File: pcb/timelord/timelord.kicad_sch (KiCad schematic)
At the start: 33 parts, among them J1 GPIO, J2 BCKP_PWR, J3 OLED, J4 EXTERNAL, J5 SMA, Q1 BC846, Q2 BC846, U2 NEO-F10T, U3 DS3231MZ

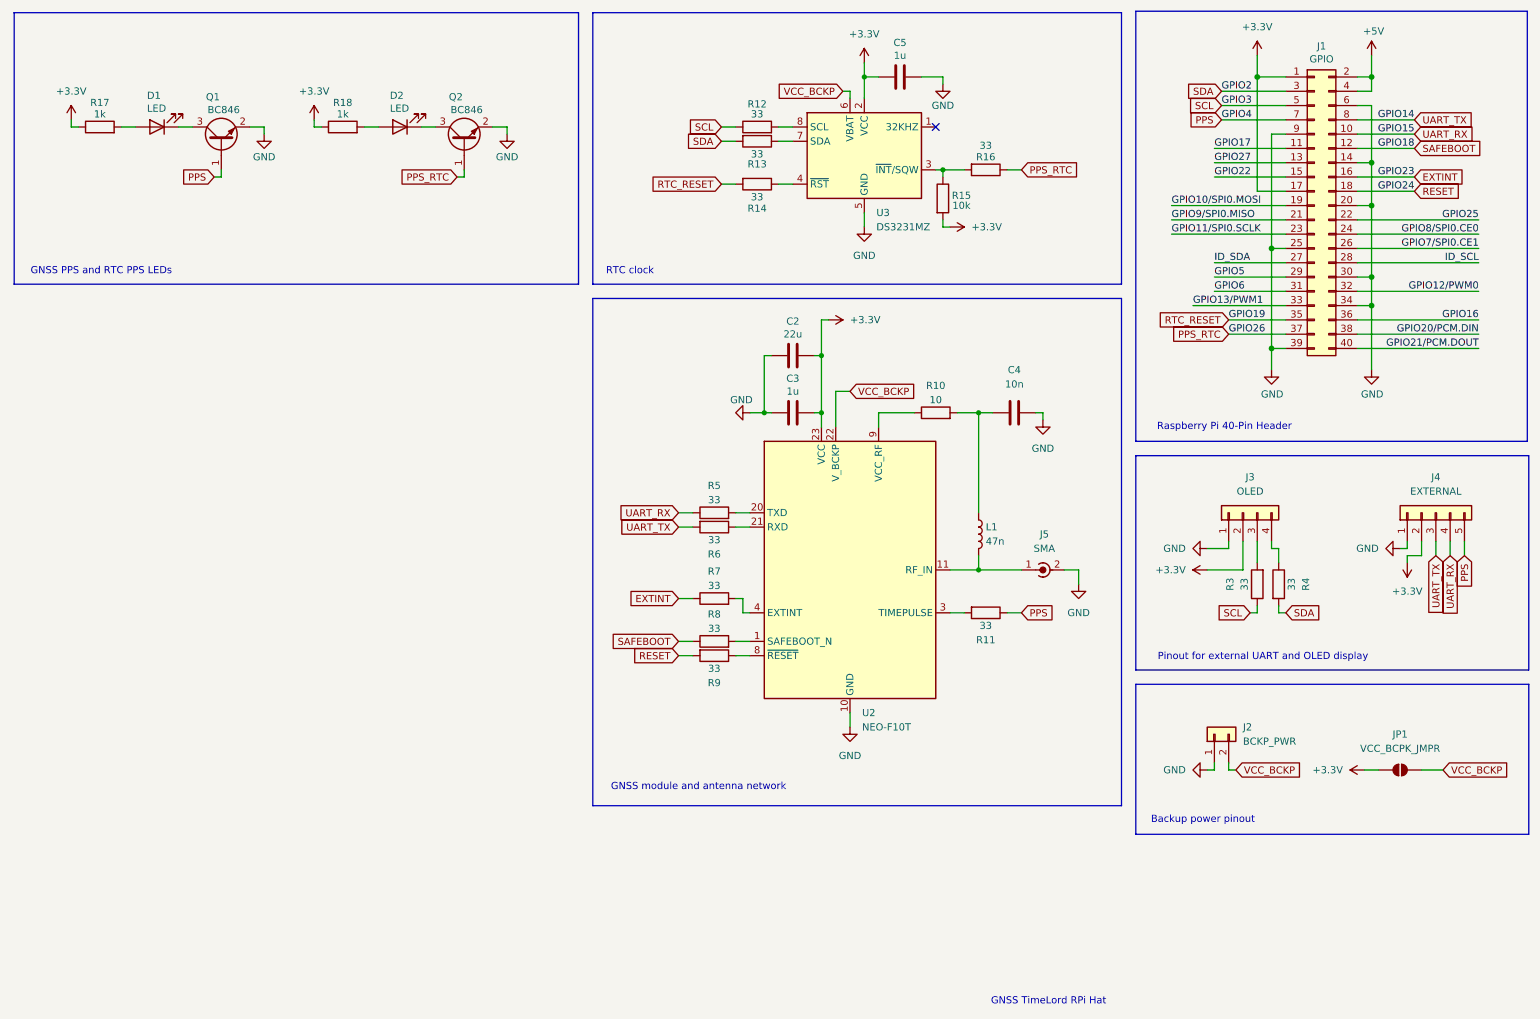
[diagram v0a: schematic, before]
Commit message: Fix MFRs and component sizing
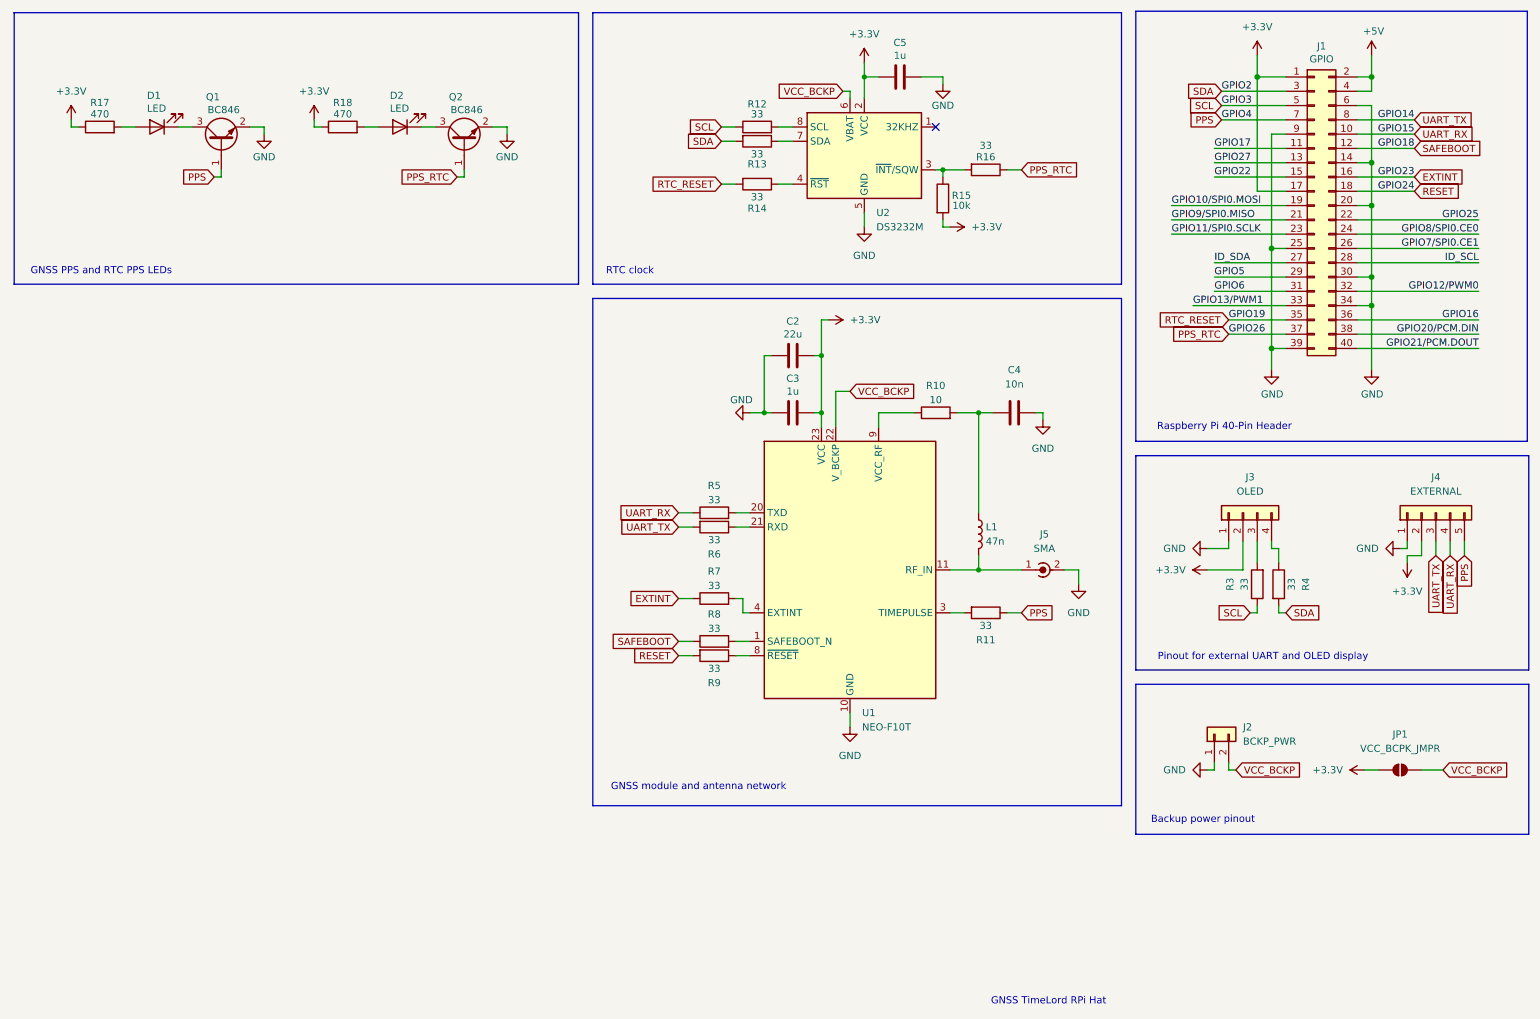
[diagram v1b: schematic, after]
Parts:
- removed U3: DS3231MZ, Package_SO:SOIC-8_3.9x4.9mm_P1.27mm, symbol Timer_RTC:DS3231MZ
- added U2: DS3232M, Package_SO:SOIC-8_3.9x4.9mm_P1.27mm, symbol Timer_RTC:DS3232M
- D1: MFR 720-KRDELPS122A5163 -> 720-KBDELPS212A6350
- J1: MFR (none) -> 485-2222
- Q1, Q2: MFR 621-1N5711W-F -> 863-BC846BLT1G
- R17, R18: value 1k -> 470; footprint Resistor_SMD:R_0805_2012Metric -> Resistor_SMD:R_0603_1608Metric; MFR 603-RT0805DRD071KL -> 603-RT0603DRD07470RL
- renumbered U2 to U1
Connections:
- net +3.3V: now also U2.2 (VCC)
- net GND: now also U2.5 (GND)
- net VCC_BCKP: now also U2.6 (VBAT)
- net at R15.1, R16.2: now also U2.3 (~{INT}/SQW)
- net at R14.1: now also U2.4 (~{RST})
- net at R13.1: now also U2.7 (SDA)
- net at R12.2: now also U2.8 (SCL)
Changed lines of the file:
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@@
 			)
 		)
+		(property "MFR" "485-2222"
+			(at 245.11 48.26 0)
+			(effects
+				(font
+					(size 1.27 1.27)
+				)
+				(hide yes)
+			)
+		)
 		(pin "1"
 		)
@@
 		(dnp no)
 		(fields_autoplaced yes)
-		(property "Reference" "U2"
+		(property "Reference" "U1"
 			(at 164.7033 138.43 0)
 			(effects
@@
 			(project ""
 				(path "/e63e39d7-6ac0-4ffd-8aa3-1841a4541b55"
-					(reference "U2")
+					(reference "U1")
 					(unit 1)
 				)
@@
 	(symbol
 		(lib_id "Device:R")
-		(at 186.69 41.91 270)
+		(at 29.21 34.29 90)
 		(unit 1)
 		(exclude_from_sim no)
@@
 		(on_board yes)
 		(dnp no)
-		(property "Reference" "R16"
-			(at 186.69 39.624 90)
+		(property "Reference" "R17"
+			(at 29.21 29.972 90)
 			(effects
 				(font
@@
 			)
 		)
-		(property "Value" "33"
-			(at 186.69 37.592 90)
+		(property "Value" "470"
+			(at 29.21 32.004 90)
 			(effects
 				(font
@@
 		)
 		(property "Footprint" "Resistor_SMD:R_0603_1608Metric"
-			(at 186.69 40.132 90)
+			(at 29.21 36.068 90)
 			(effects
 				(font
@@
 		)
 		(property "Datasheet" "~"
-			(at 186.69 41.91 0)
+			(at 29.21 34.29 0)
 			(effects
 				(font
@@
 		)
 		(property "Description" "Resistor"
-			(at 186.69 41.91 0)
+			(at 29.21 34.29 0)
 			(effects
 				(font
@@
 			)
 		)
-		(property "MFR" "603-RT0603FRE0733RL"
-			(at 186.69 41.91 90)
+		(property "MFR" "603-RT0603DRD07470RL"
+			(at 29.21 34.29 90)
 			(effects
 				(font
@@
 		)
 		(instances
-			(project ""
+			(project "timelord"
 				(path "/e63e39d7-6ac0-4ffd-8aa3-1841a4541b55"
-					(reference "R16")
+					(reference "R17")
 					(unit 1)
 				)
@@
 	)
 	(symbol
-		(lib_id "power:+3.3V")
-		(at 226.06 113.03 90)
+		(lib_id "Device:R")
+		(at 186.69 41.91 270)
 		(unit 1)
 		(exclude_from_sim no)
@@
 		(on_board yes)
 		(dnp no)
-		(fields_autoplaced yes)
-		(property "Reference" "#PWR0119"
-			(at 229.87 113.03 0)
+		(property "Reference" "R16"
+			(at 186.69 39.624 90)
 			(effects
 				(font
 					(size 1.27 1.27)
 				)
-				(hide yes)
 			)
 		)
-		(property "Value" "+3.3V"
-			(at 222.25 113.0299 90)
+		(property "Value" "33"
+			(at 186.69 37.592 90)
 			(effects
 				(font
 					(size 1.27 1.27)
 				)
-				(justify left)
 			)
 		)
-		(property "Footprint" ""
-			(at 226.06 113.03 0)
+		(property "Footprint" "Resistor_SMD:R_0603_1608Metric"
+			(at 186.69 40.132 90)
 			(effects
 				(font
@@
 			)
 		)
-		(property "Datasheet" ""
-			(at 226.06 113.03 0)
+		(property "Datasheet" "~"
+			(at 186.69 41.91 0)
 			(effects
 				(font
@@
 			)
 		)
-		(property "Description" "Power symbol creates a global label with name \"+3.3V\""
-			(at 226.06 113.03 0)
+		(property "Description" "Resistor"
+			(at 186.69 41.91 0)
+			(effects
+				(font
+					(size 1.27 1.27)
+				)
+				(hide yes)
+			)
+		)
+		(property "MFR" "603-RT0603FRE0733RL"
+			(at 186.69 41.91 90)
 			(effects
 				(font
@@
 		(pin "1"
 		)
+		(pin "2"
+		)
 		(instances
-			(project "timelord2"
+			(project ""
 				(path "/e63e39d7-6ac0-4ffd-8aa3-1841a4541b55"
-					(reference "#PWR0119")
+					(reference "R16")
 					(unit 1)
 				)
@@
 	)
 	(symbol
-		(lib_id "Device:R")
-		(at 29.21 34.29 90)
+		(lib_id "power:+3.3V")
+		(at 226.06 113.03 90)
 		(unit 1)
 		(exclude_from_sim no)
@@
 		(on_board yes)
 		(dnp no)
-		(property "Reference" "R17"
-			(at 29.21 29.972 90)
-			(effects
-				(font
-					(size 1.27 1.27)
-				)
-			)
-		)
-		(property "Value" "1k"
-			(at 29.21 32.004 90)
+		(fields_autoplaced yes)
+		(property "Reference" "#PWR0119"
+			(at 229.87 113.03 0)
 			(effects
 				(font
 					(size 1.27 1.27)
 				)
+				(hide yes)
 			)
 		)
-		(property "Footprint" "Resistor_SMD:R_0805_2012Metric"
-			(at 29.21 36.068 90)
+		(property "Value" "+3.3V"
+			(at 222.25 113.0299 90)
 			(effects
 				(font
 					(size 1.27 1.27)
 				)
-				(hide yes)
+				(justify left)
 			)
 		)
-		(property "Datasheet" "~"
-			(at 29.21 34.29 0)
+		(property "Footprint" ""
+			(at 226.06 113.03 0)
 			(effects
 				(font
@@
 			)
 		)
-		(property "Description" "Resistor"
-			(at 29.21 34.29 0)
+		(property "Datasheet" ""
+			(at 226.06 113.03 0)
 			(effects
 				(font
@@
 			)
 		)
-		(property "MFR" "603-RT0805DRD071KL"
-			(at 29.21 34.29 90)
+		(property "Description" "Power symbol creates a global label with name \"+3.3V\""
+			(at 226.06 113.03 0)
 			(effects
 				(font
@@
 		(pin "1"
 		)
-		(pin "2"
-		)
 		(instances
 			(project "timelord2"
 				(path "/e63e39d7-6ac0-4ffd-8aa3-1841a4541b55"
-					(reference "R17")
+					(reference "#PWR0119")
 					(unit 1)
 				)
@@
 			)
 		)
-		(property "MFR" "720-KRDELPS122A5163"
+		(property "MFR" "720-KBDELPS212A6350"
 			(at 39.37 34.29 0)
 			(effects
@@
 			)
 		)
-		(property "Value" "1k"
+		(property "Value" "470"
 			(at 72.39 32.004 90)
 			(effects
@@
 			)
 		)
-		(property "Footprint" "Resistor_SMD:R_0805_2012Metric"
+		(property "Footprint" "Resistor_SMD:R_0603_1608Metric"
 			(at 72.39 36.068 90)
 			(effects
@@
 			)
 		)
-		(property "MFR" "603-RT0805DRD071KL"
+		(property "MFR" "603-RT0603DRD07470RL"
 			(at 72.39 34.29 90)
 			(effects
@@
 	)
 	(symbol
-		(lib_id "Timer_RTC:DS3231MZ")
-		(at 165.1 39.37 0)
-		(unit 1)
-		(exclude_from_sim no)
-		(in_bom yes)
-		(on_board yes)
-		(dnp no)
-		(fields_autoplaced yes)
-		(property "Reference" "U3"
-			(at 167.2433 49.53 0)
-			(effects
-				(font
-					(size 1.27 1.27)
-				)
-				(justify left)
-			)
-		)
-		(property "Value" "DS3231MZ"
-			(at 167.2433 52.07 0)
-			(effects
-				(font
-					(size 1.27 1.27)
-				)
-				(justify left)
-			)
-		)
-		(property "Footprint" "Package_SO:SOIC-8_3.9x4.9mm_P1.27mm"
-			(at 165.1 52.07 0)
-			(effects
-				(font
-					(size 1.27 1.27)
-				)
-				(hide yes)
-			)
-		)
-		(property "Datasheet" "http://datasheets.maximintegrated.com/en/ds/DS3231M.pdf"
-			(at 165.1 54.61 0)
-			(effects
-				(font
-					(size 1.27 1.27)
-				)
-				(hide yes)
-			)
-		)
-		(property "Description" "±5ppm, I2C Real-Time Clock SOIC-8"
-			(at 165.1 39.37 0)
-			(effects
-				(font
-					(size 1.27 1.27)
-				)
-				(hide yes)
-			)
-		)
-		(pin "6"
-		)
-		(pin "8"
-		)
-		(pin "2"
-		)
-		(pin "5"
-		)
-		(pin "4"
-		)
-		(pin "3"
-		)
-		(pin "7"
-		)
-		(pin "1"
-		)
-		(instances
-			(project ""
-				(path "/2c3bf53d-e449-43cf-bd3c-975c2dd5bd35"
-					(reference "U2")
-					(unit 1)
-				)
-			)
-			(project ""
-				(path "/e63e39d7-6ac0-4ffd-8aa3-1841a4541b55"
-					(reference "U3")
-					(unit 1)
-				)
-			)
-		)
-	)
-	(symbol
 		(lib_id "Jumper:SolderJumper_2_Open")
 		(at 260.35 148.59 0)
@@
 			)
 		)
-		(property "MFR" "621-1N5711W-F"
+		(property "MFR" "863-BC846BLT1G"
 			(at 93.98 36.83 90)
 			(effects
@@
 	)
 	(symbol
+		(lib_id "Timer_RTC:DS3232M")
+		(at 165.1 39.37 0)
+		(unit 1)
+		(exclude_from_sim no)
+		(in_bom yes)
+		(on_board yes)
+		(dnp no)
+		(fields_autoplaced yes)
+		(property "Reference" "U2"
+			(at 167.2433 49.53 0)
+			(effects
+				(font
+					(size 1.27 1.27)
+				)
+				(justify left)
+			)
+		)
+		(property "Value" "DS3232M"
+			(at 167.2433 52.07 0)
+			(effects
+				(font
+					(size 1.27 1.27)
+				)
+				(justify left)
+			)
+		)
+		(property "Footprint" "Package_SO:SOIC-8_3.9x4.9mm_P1.27mm"
+			(at 166.37 52.07 0)
+			(effects
+				(font
+					(size 1.27 1.27)
+				)
+				(hide yes)
+			)
+		)
+		(property "Datasheet" "http://datasheets.maximintegrated.com/en/ds/DS3232M.pdf"
+			(at 171.958 35.56 0)
+			(effects
+				(font
+					(size 1.27 1.27)
+				)
+				(hide yes)
+			)
+		)
+		(property "Description" "±5ppm, I2C Real-Time Clock with SRAM SOIC-8"
+			(at 165.1 39.37 0)
+			(effects
+				(font
+					(size 1.27 1.27)
+				)
+				(hide yes)
+			)
+		)
+		(property "MFR" "700-DS3232MZ+TRL"
+			(at 165.1 39.37 0)
+			(effects
+				(font
+					(size 1.27 1.27)
+				)
+				(hide yes)
+			)
+		)
+		(pin "8"
+		)
+		(pin "6"
+		)
+		(pin "2"
+		)
+		(pin "1"
+		)
+		(pin "4"
+		)
+		(pin "3"
+		)
+		(pin "5"
+		)
+		(pin "7"
+		)
+		(instances
+			(project ""
+				(path "/e63e39d7-6ac0-4ffd-8aa3-1841a4541b55"
+					(reference "U2")
+					(unit 1)
+				)
+			)
+		)
+	)
+	(symbol
 		(lib_id "Connector_Generic:Conn_01x05")
 		(at 266.7 102.87 90)
@@
 			)
 		)
-		(property "MFR" "621-1N5711W-F"
+		(property "MFR" "863-BC846BLT1G"
 			(at 50.8 36.83 90)
 			(effects

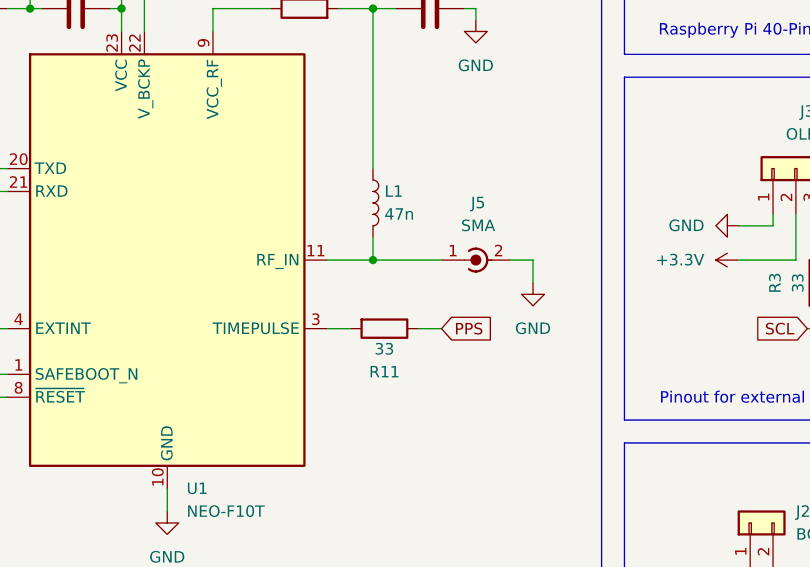
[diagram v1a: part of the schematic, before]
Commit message: Reworked RF part of the PCB
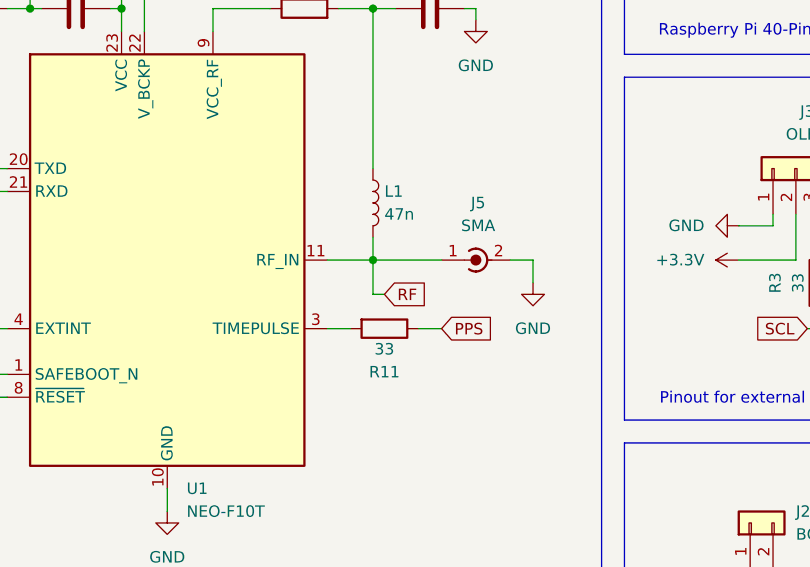
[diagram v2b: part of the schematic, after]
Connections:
- net RF: now reaches J5.1 (In), L1.2, U1.11 (RF_IN)

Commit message: Add SMA PPS connector and change 5V plane to GND plane
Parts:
- added J6: SMA, Connector_Coaxial:SMA_Amphenol_132289_EdgeMount, symbol Connector:Conn_Coaxial_Power
- added R1, R19, R2: 0, Resistor_SMD:R_0603_1608Metric, symbol Device:R
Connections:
- net GND: now also J6.2 (Ext)
- net PPS: now also R2.2
- net PPS_RTC: now also R1.2
- net GPIO17 renamed PPS_EXT
- net PPS_EXT: now also R19.2
- new net: J6.1 (In), R1.1, R19.1, R2.1
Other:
- note added: "PPS SMA connector"

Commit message: Changes
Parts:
- added J7: I2C pinout, Connector_PinSocket_2.54mm:PinSocket_1x04_P2.54mm_Vertical, symbol Connector_Generic:Conn_01x04
- added J8: UART3, Connector_PinHeader_2.54mm:PinHeader_1x03_P2.54mm_Vertical, symbol Connector_Generic:Conn_01x03
- added J9: UART4, Connector_PinHeader_2.54mm:PinHeader_1x03_P2.54mm_Vertical, symbol Connector_Generic:Conn_01x03
- added R20, R21: 33, Resistor_SMD:R_0603_1608Metric, symbol Device:R
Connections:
- net +3.3V: now also J7.2 (Pin_2)
- net GND: now also J7.1 (Pin_1), J8.1 (Pin_1), J9.1 (Pin_1)
- net SCL: now also R20.1
- net SDA: now also R21.2
- net GPIO10/SPI0.MOSI renamed GPIO10
- net GPIO11/SPI0.SCLK renamed GPIO11
- net GPIO12/PWM0 renamed UART4_TX
- net UART4_TX: now also J9.3 (Pin_3)
- net GPIO13/PWM1 renamed UART4_RX
- net UART4_RX: now also J9.2 (Pin_2)
- net GPIO7/SPI0.CE1 renamed GPIO7
- net GPIO8/SPI0.CE0 renamed UART3_TX
- net UART3_TX: now also J8.3 (Pin_3)
- net GPIO9/SPI0.MISO renamed UART3_RX
- net UART3_RX: now also J8.2 (Pin_2)
- net UART_RX renamed UART0_RX
- net UART_TX renamed UART0_TX
- new net: J7.3 (Pin_3), R20.2
- new net: J7.4 (Pin_4), R21.1
